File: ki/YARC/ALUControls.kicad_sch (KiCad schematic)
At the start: 11 parts, among them U123 74LS32, U124 74LS08, U125 74LS08, U126 74LS00, U127 74LS74, U128 74LS157, U129 74LS574, U130 74LS157, U131 74LS245

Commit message: Various corrections and minor improvements
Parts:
- added U107: 74HC00, symbol 74xx:74HC00
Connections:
- net FREG.C: now also U107.9; no longer U124.2
- new net: U107.12, U107.13, U107.8
- new net: U107.11, U124.2
- new net PHI_1_PLS: U107.10
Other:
- note added: "PHI1 CIN"
- note added: "PHI2 CIN"
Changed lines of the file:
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@@
   (junction (at 167.64 132.08) (diameter 0) (color 0 0 0 0)
   )
+  (junction (at 58.42 147.32) (diameter 0) (color 0 0 0 0)
+  )
   (junction (at 152.4 114.3) (diameter 0) (color 0 0 0 0)
   )
@@
     (stroke (width 0) (type default) (color 0 0 0 0))
   )
+  (wire (pts (xy 83.82 144.78) (xy 88.9 144.78))
+    (stroke (width 0) (type default) (color 0 0 0 0))
+  )
   (bus (pts (xy 231.14 33.02) (xy 251.46 33.02))
     (stroke (width 0) (type default) (color 0 0 0 0))
@@
     (stroke (width 0) (type default) (color 0 0 0 0))
   )
-  (wire (pts (xy 33.02 147.32) (xy 114.3 147.32))
-    (stroke (width 0) (type default) (color 0 0 0 0))
-  )
   (wire (pts (xy 190.5 66.04) (xy 198.12 66.04))
     (stroke (width 0) (type default) (color 0 0 0 0))
@@
     (stroke (width 0) (type default) (color 0 0 0 0))
   )
+  (wire (pts (xy 58.42 144.78) (xy 58.42 147.32))
+    (stroke (width 0) (type default) (color 0 0 0 0))
+  )
   (wire (pts (xy 48.26 127) (xy 48.26 119.38))
     (stroke (width 0) (type default) (color 0 0 0 0))
   )
+  (wire (pts (xy 43.18 147.32) (xy 33.02 147.32))
+    (stroke (width 0) (type default) (color 0 0 0 0))
+  )
   (wire (pts (xy 190.5 50.8) (xy 198.12 50.8))
     (stroke (width 0) (type default) (color 0 0 0 0))
@@
     (stroke (width 0) (type default) (color 0 0 0 0))
   )
-  (wire (pts (xy 114.3 147.32) (xy 114.3 88.9))
+  (wire (pts (xy 114.3 88.9) (xy 114.3 149.86))
     (stroke (width 0) (type default) (color 0 0 0 0))
   )
@@
     (stroke (width 0) (type default) (color 0 0 0 0))
   )
+  (wire (pts (xy 68.58 147.32) (xy 58.42 147.32))
+    (stroke (width 0) (type default) (color 0 0 0 0))
+  )
   (bus (pts (xy 139.7 101.6) (xy 139.7 104.14))
     (stroke (width 0) (type default) (color 0 0 0 0))
@@
     (stroke (width 0) (type default) (color 0 0 0 0))
   )
+  (wire (pts (xy 83.82 149.86) (xy 114.3 149.86))
+    (stroke (width 0) (type default) (color 0 0 0 0))
+  )
   (wire (pts (xy 198.12 111.76) (xy 198.12 114.3))
     (stroke (width 0) (type default) (color 0 0 0 0))
@@
     (stroke (width 0) (type default) (color 0 0 0 0))
   )
+  (wire (pts (xy 58.42 147.32) (xy 58.42 149.86))
+    (stroke (width 0) (type default) (color 0 0 0 0))
+  )
   (wire (pts (xy 190.5 132.08) (xy 167.64 132.08))
     (stroke (width 0) (type default) (color 0 0 0 0))
@@
   )
   (text "U130 AND U131 ARE\nIN THE GENERAL\nREGISTERS AREA." (at 236.22 134.62 0)
+    (effects (font (size 1.27 1.27)) (justify left bottom))
+  )
+  (text "PHI2 CIN" (at 81.28 121.92 0)
+    (effects (font (size 1.27 1.27)) (justify left bottom))
+  )
+  (text "PHI1 CIN" (at 63.5 137.16 0)
     (effects (font (size 1.27 1.27)) (justify left bottom))
   )
@@
     (effects (font (size 1.27 1.27)) (justify left bottom))
   )
+  (label "FREG.C" (at 91.44 149.86 0)
+    (effects (font (size 1.27 1.27)) (justify left bottom))
+  )
   (label "FMUXIN.N" (at 223.52 58.42 0)
     (effects (font (size 1.27 1.27)) (justify left bottom))
@@
   )
   (label "SYSDATA[0..15]" (at 231.14 33.02 0)
-    (effects (font (size 1.27 1.27)) (justify left bottom))
-  )
-  (label "FREG.C" (at 35.56 139.7 0)
     (effects (font (size 1.27 1.27)) (justify left bottom))
   )
@@
     (effects (font (size 1.27 1.27)) (justify left))
     (property "Intersheet References" "${INTERSHEET_REFS}" (id 0) (at 176.9474 38.0206 0)
+      (effects (font (size 1.27 1.27)) (justify left) hide)
+    )
+  )
+  (global_label "PHI_1_PLS" (shape input) (at 88.9 144.78 0) (fields_autoplaced)
+    (effects (font (size 1.27 1.27)) (justify left))
+    (property "Intersheet References" "${INTERSHEET_REFS}" (id 0) (at 101.1707 144.7006 0)
       (effects (font (size 1.27 1.27)) (justify left) hide)
     )
@@
   (symbol (lib_id "74xx:74LS32") (at 43.18 157.48 0) (unit 4)
     (in_bom yes) (on_board yes)
-    (property "Reference" "U123" (id 0) (at 48.26 152.4 0))
+    (property "Reference" "U123" (id 0) (at 50.8 160.02 0))
     (property "Value" "74LS32" (id 1) (at 43.18 157.48 0))
     (property "Footprint" "" (id 2) (at 43.18 157.48 0)
@@
     (pin "1")
   )
+  (symbol (lib_id "74xx:74HC00") (at 76.2 147.32 180) (unit 3)
+    (in_bom yes) (on_board yes)
+    (property "Reference" "U107" (id 0) (at 71.12 152.4 0))
+    (property "Value" "74HC00" (id 1) (at 76.2 147.32 0))
+    (property "Footprint" "" (id 2) (at 76.2 147.32 0)
+      (effects (font (size 1.27 1.27)) hide)
+    )
+    (property "Datasheet" "http://www.ti.com/lit/gpn/sn74hc00" (id 3) (at 76.2 147.32 0)
+      (effects (font (size 1.27 1.27)) hide)
+    )
+    (pin "10")
+    (pin "8")
+    (pin "9")
+  )
   (symbol (lib_id "74xx:74LS74") (at 88.9 33.02 0) (unit 1)
     (in_bom yes) (on_board yes)
@@
     (pin "1")
   )
+  (symbol (lib_id "74xx:74HC00") (at 50.8 147.32 180) (unit 4)
+    (in_bom yes) (on_board yes)
+    (property "Reference" "U107" (id 0) (at 50.8 144.78 0))
+    (property "Value" "74HC00" (id 1) (at 50.8 147.32 0))
+    (property "Footprint" "" (id 2) (at 50.8 147.32 0)
+      (effects (font (size 1.27 1.27)) hide)
+    )
+    (property "Datasheet" "http://www.ti.com/lit/gpn/sn74hc00" (id 3) (at 50.8 147.32 0)
+      (effects (font (size 1.27 1.27)) hide)
+    )
+    (pin "11")
+    (pin "12")
+    (pin "13")
+  )
   (symbol (lib_id "74xx:74LS08") (at 50.8 137.16 0) (unit 1)

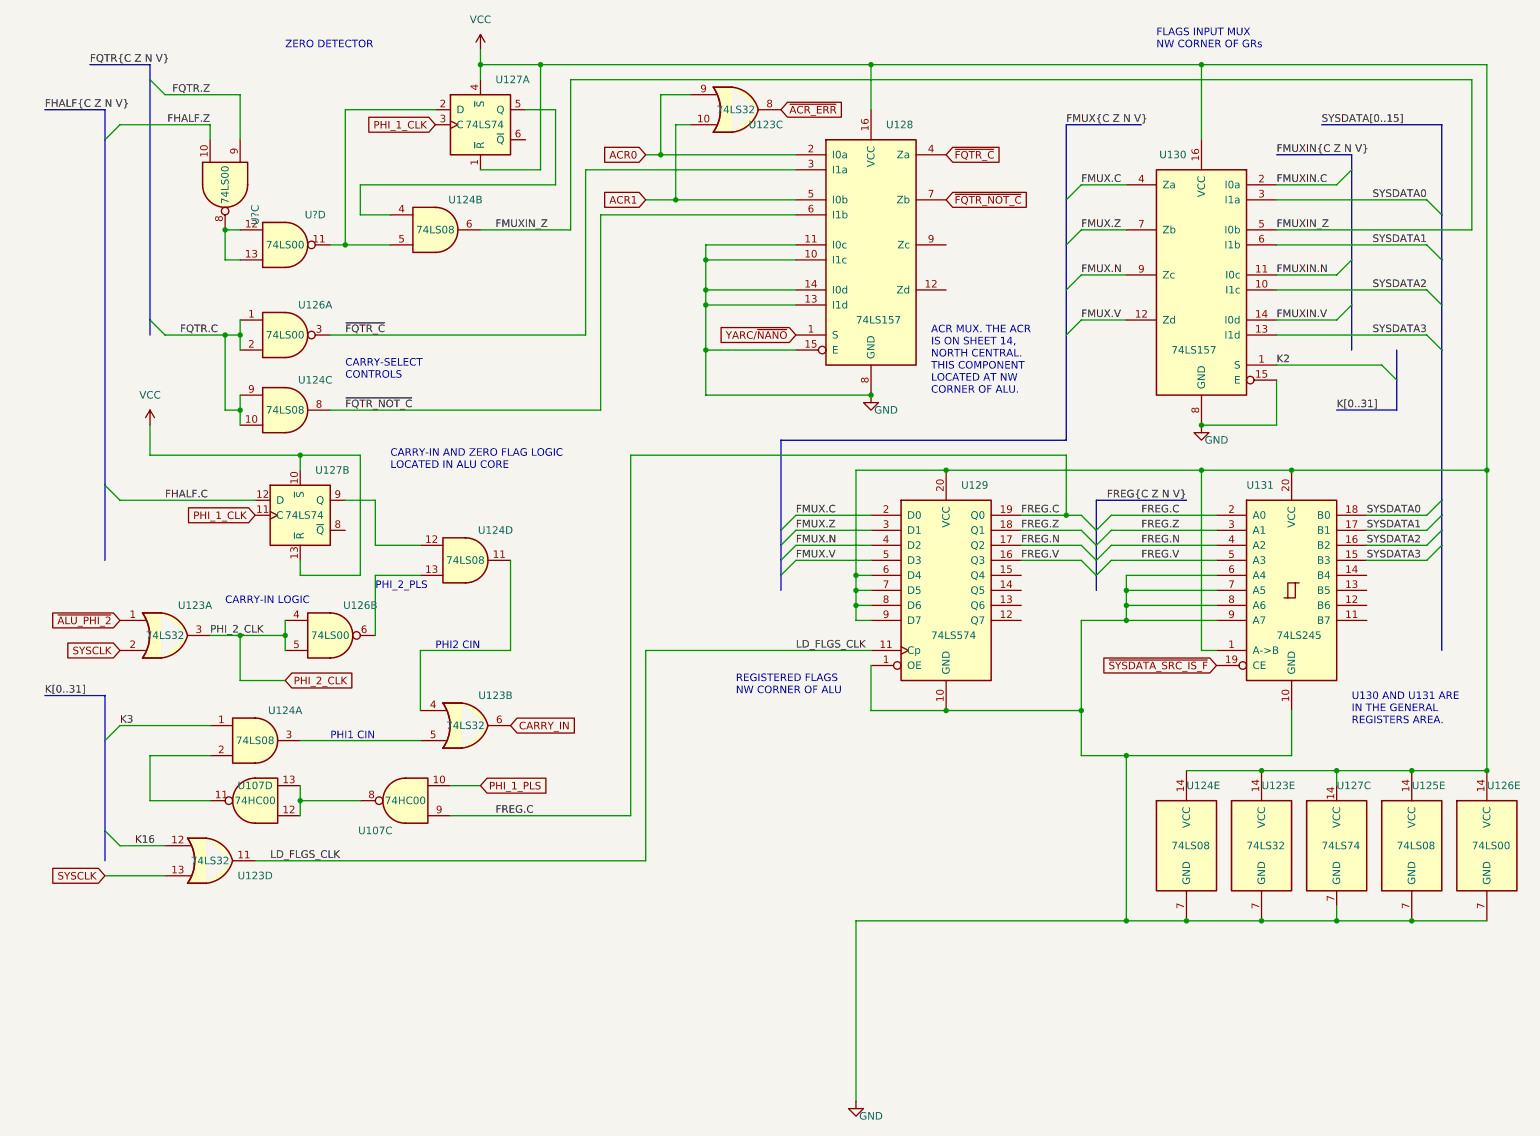
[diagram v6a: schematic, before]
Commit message: Updates for ad hoc wiring changes
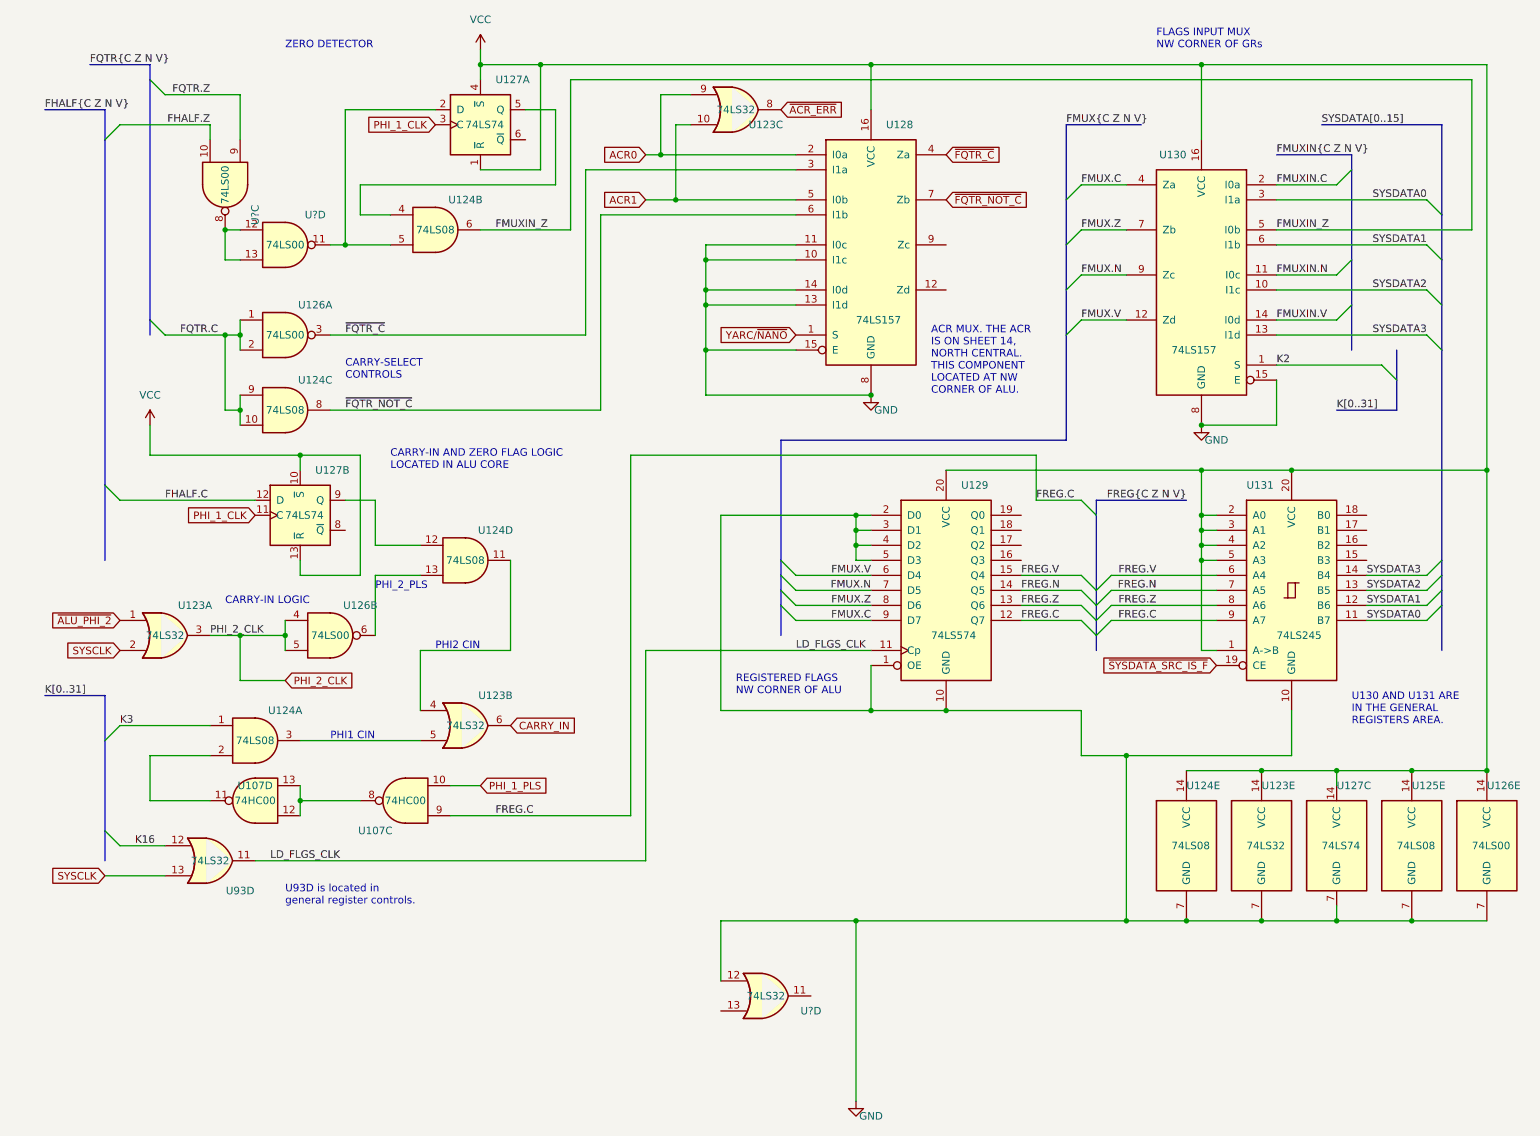
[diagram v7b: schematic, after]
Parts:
- removed unit 4 of U123
- added U93, U?: 74LS32, symbol 74xx:74LS32
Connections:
- net FMUX.C: now also U129.9 (D7); no longer U129.2 (D0)
- net FMUX.N: now also U129.7 (D5); no longer U129.4 (D2)
- net FMUX.V: now also U129.6 (D4); no longer U129.5 (D3)
- net FMUX.Z: now also U129.8 (D6); no longer U129.3 (D1)
- net FREG.C: now also U129.12 (Q7), U131.9 (A7); no longer U129.19 (Q0), U131.2 (A0)
- net FREG.N: now also U129.14 (Q5), U131.7 (A5); no longer U129.17 (Q2), U131.4 (A2)
- net FREG.V: now also U129.15 (Q4), U131.6 (A4); no longer U129.16 (Q3), U131.5 (A3)
- net FREG.Z: now also U129.13 (Q6), U131.8 (A6); no longer U129.18 (Q1), U131.3 (A1)
- net GND: now also U129.2 (D0), U129.3 (D1), U129.4 (D2), U129.5 (D3), U?.12; no longer U131.6 (A4), U131.7 (A5), U131.8 (A6), U131.9 (A7)
- net K16: now also U93.12
- net LD_FLGS_CLK: now also U93.11
- net SYSCLK: now also U93.13
- net SYSDATA0: now also U131.11 (B7); no longer U131.18 (B0)
- net SYSDATA1: now also U131.12 (B6); no longer U131.17 (B1)
- net SYSDATA2: now also U131.13 (B5); no longer U131.16 (B2)
- net SYSDATA3: now also U131.14 (B4); no longer U131.15 (B3)
- net VCC: now also U131.2 (A0), U131.3 (A1), U131.4 (A2), U131.5 (A3); no longer U129.6 (D4), U129.7 (D5), U129.8 (D6), U129.9 (D7)
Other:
- note added: "U93D is located in general register controls."

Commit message: Redesign of ALU control logic
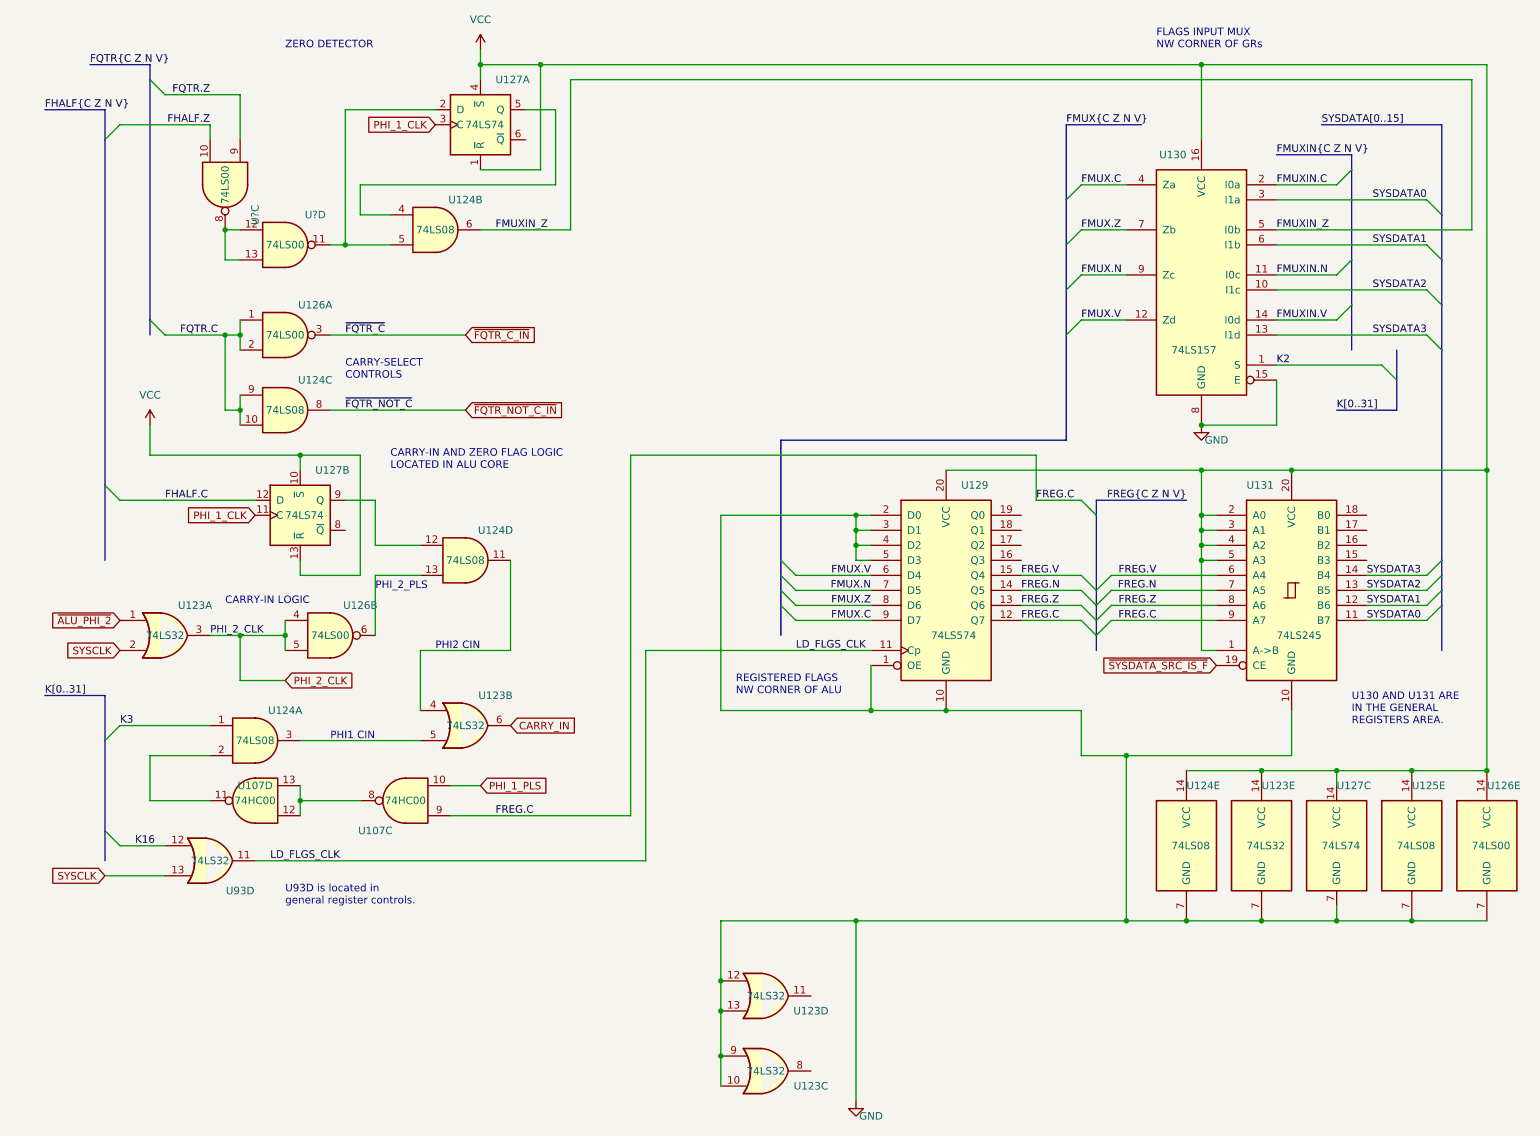
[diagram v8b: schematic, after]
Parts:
- removed U128: 74LS157, symbol 74xx:74LS157
- gave numbers to parts that had none: 1
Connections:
- net ACR0 is gone; now on net GND: U123.9
- net ACR1 is gone; now on net GND: U123.10
- net GND: now also U123.13
- net ~{ACR_ERR}: no longer names the net of U123.8
- net ~{FQTR_C} renamed ~{FQTR_C_IN}
- net ~{FQTR_NOT_C} renamed ~{FQTR_NOT_C_IN}
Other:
- note removed: "ACR MUX. THE ACR IS ON SHEET 14, NORTH CENTRAL. THIS COMPONENT LOCATED AT NW CORNER OF ALU."
